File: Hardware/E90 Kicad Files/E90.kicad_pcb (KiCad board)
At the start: 2 copper layers, 93 parts, among them J1 Power Connector Conn_01x02, J10 SDIN Jumper, J11 CS_SDOUT Pre Buffer Test Point, J12 SDOUT Jumper, J13 Audio Connector In Conn_01x03, J14 Conn_02x06_Odd_Even, J15 CS Passthru Jumper Conn_01x02, J16 CS Power Switch Conn_01x02, J17 I2S SDIN Bypass Jumper Conn_0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, J18 PMOD Passthru, J19 I2S SDOUT Bypass Conn_01x02, J2 SWD Connector Conn_02x03, J3 Power Test Point Conn_01x02, J4 BOOT0 Test Point, J6 Audio Connector Out Conn_01x03, J7 MCLK Jumper, J8 WS Jumper, J9 SCLK Jumper, U1 AMS1117-3.3, U2 CS4344_CZZ, U3 NC7SZ125P5, U4 CS5343_CZZ, U5 STM32F407VGT60

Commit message: refactoring PCB
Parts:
- moved C35 214.2 mm to (72.1, 116.1), turned to 180 degrees
- moved C3 206.4 mm to (66.3, 102.3), turned to 270 degrees
- moved C4 204.3 mm to (70.9, 99.6)
- moved FB2 195.6 mm to (66.8, 99.8), turned to 180 degrees
- moved C10 195.2 mm to (77.5, 106.9), turned to 180 degrees
- moved C33 195.0 mm to (77.7, 116.3), turned to 270 degrees
- moved R4 189.8 mm to (90.0, 104.6)
- moved C31 187.4 mm to (87.3, 111.1), turned to 180 degrees
- moved J12 185.3 mm to (75.0, 92.5)
- moved C12 185.1 mm to (92.8, 105.4), turned to 90 degrees
- moved C11 182.5 mm to (92.7, 101.5), turned to 270 degrees
- moved C6 181.3 mm to (84.3, 102.4), turned to 180 degrees
- moved C34 181.1 mm to (75.4, 116.1), turned to 180 degrees
- moved C32 180.9 mm to (87.4, 113.3), turned to 180 degrees
- moved R12 175.0 mm to (89.9, 110.3), turned to 270 degrees
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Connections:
- C23 pad 1: CS_POWER -> +3V3
- C3 pad 1: CS_POWER -> +3V3
- FB2 pad 2: CS_POWER -> +3V3
- FB4 pad 2: CS_POWER -> +3V3
- J6 pad 1: Net-(C12-Pad2) -> Net-(C11-Pad2)
- J6 pad 2: Net-(C11-Pad2) -> Net-(C12-Pad2)
- R11 pad 1: Net-(J13-Pad1) -> Net-(J13-Pad2)
- R9 pad 1: Net-(J13-Pad2) -> Net-(J13-Pad1)
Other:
- board outline added: 50 x 70 mm

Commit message: pcb
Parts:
- removed J16: CS Power Switch Conn_01x02, Connector_PinHeader_2.54mm:PinHeader_1x02_P2.54mm_Vertical
- moved R16 111.3 mm to (58.9, 93.8), turned to 270 degrees
- moved D5 110.5 mm to (60.5, 101.2)
- moved R15 105.6 mm to (60.9, 93.8), turned to 270 degrees
- moved C14 100.7 mm to (64.5, 78.2), turned to 270 degrees
- moved C13 99.9 mm to (63.1, 78.2), turned to 270 degrees
- moved C30 98.3 mm to (64.7, 76.2), turned to 180 degrees
- moved R10 97.8 mm to (68.3, 115.0), turned to 90 degrees
- moved U3 96.3 mm to (63.5, 110.0)
- moved C21 94.2 mm to (64.8, 68.4), turned to 180 degrees
- moved C16 92.5 mm to (69.6, 60.2)
- moved R18 91.6 mm to (54.8, 93.8), turned to 270 degrees
- moved C24 90.3 mm to (79.7, 106.2)
- moved C38 88.7 mm to (60.6, 66.6)
- moved C15 85.9 mm to (65.5, 62.2), turned to 180 degrees
- moved C29 83.9 mm to (64.2, 74.8), turned to 180 degrees
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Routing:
- net +3V3: track 0.00 -> 68.8 mm, vias 0 -> 17
- net CS_MCLK: track 0.00 -> 65.9 mm
- net CS_WS: track 0.00 -> 57.6 mm
- net GND: track 0.00 -> 57.2 mm, vias 0 -> 45
- net CS_CLK: track 0.00 -> 49.6 mm
- net Net-(R18-Pad1): track 0.00 -> 42.1 mm, vias 0 -> 2
- net Net-(R17-Pad2): track 0.00 -> 39.5 mm, vias 0 -> 2
- net Net-(R16-Pad1): track 0.00 -> 37.0 mm, vias 0 -> 2
- net Net-(R15-Pad1): track 0.00 -> 34.3 mm, vias 0 -> 2
- net NRST: track 0.00 -> 34.2 mm, vias 0 -> 1
- net CS_SDOUT: track 0.00 -> 33.0 mm
- net PMOD_CLK: track 0.00 -> 24.9 mm
- net SWO: track 0.00 -> 24.8 mm
- net Net-(D3-Pad2): track 0.00 -> 24.3 mm
- net PMOD_WS: track 0.00 -> 21.5 mm
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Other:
- copper layers 2 -> 4

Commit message: finished pcb 1.0
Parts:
- moved J3 33.8 mm to (54.0, 63.0), turned to 0 degrees
- moved J1 5.42 mm to (57.5, 54.0), turned to 90 degrees
- moved J2 3.99 mm to (93.2, 59.7)
- moved R20 2.65 mm to (75.3, 80.2), turned to 180 degrees
- moved C13 1.45 mm to (64.0, 79.3)
- moved C14 1.26 mm to (65.2, 79.3)
- moved R8 1.19 mm to (66.9, 79.2)
- moved C30 1.17 mm to (64.8, 77.4)
- moved C29 1.07 mm to (64.4, 75.8)
- moved D1 0.76 mm to (59.5, 59.7)
- moved C22 0.72 mm to (64.8, 65.8)
- moved C21 0.60 mm to (65.0, 67.9), turned to 90 degrees
- moved C19 0.49 mm to (69.8, 79.7)
- moved C20 0.46 mm to (64.9, 73.8), turned to 270 degrees
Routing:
- net GND: track 57.2 -> 92.3 mm, vias 45 -> 64
- net PMOD_SDOUT: track 11.6 -> 46.6 mm
- net PMOD_SDIN: track 12.1 -> 35.1 mm
- net +3V3: track 68.8 -> 85.7 mm, vias 17 -> 26
- net CS_SDIN: track 10.4 -> 25.5 mm
- net +3.3VA: track 5.96 -> 14.1 mm
- net SWO: track 24.8 -> 30.0 mm
- net SWDIO: track 17.9 -> 13.6 mm
- net SWCLK: track 15.6 -> 12.1 mm
- net VCC: track 3.64 -> 6.24 mm
- net BOOT1: track 0.00 -> 2.58 mm
- net Net-(C27-Pad1): track 0.00 -> 2.52 mm
- net Net-(C12-Pad2): track 6.00 -> 8.02 mm
- net Net-(C39-Pad1): track 1.99 -> 3.94 mm
- net Net-(C29-Pad1): track 8.74 -> 6.97 mm
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- added copper zone on In2.Cu, net +3V3
- added copper zone on In1.Cu, net GND
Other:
- outline, holes or cut-outs redrawn

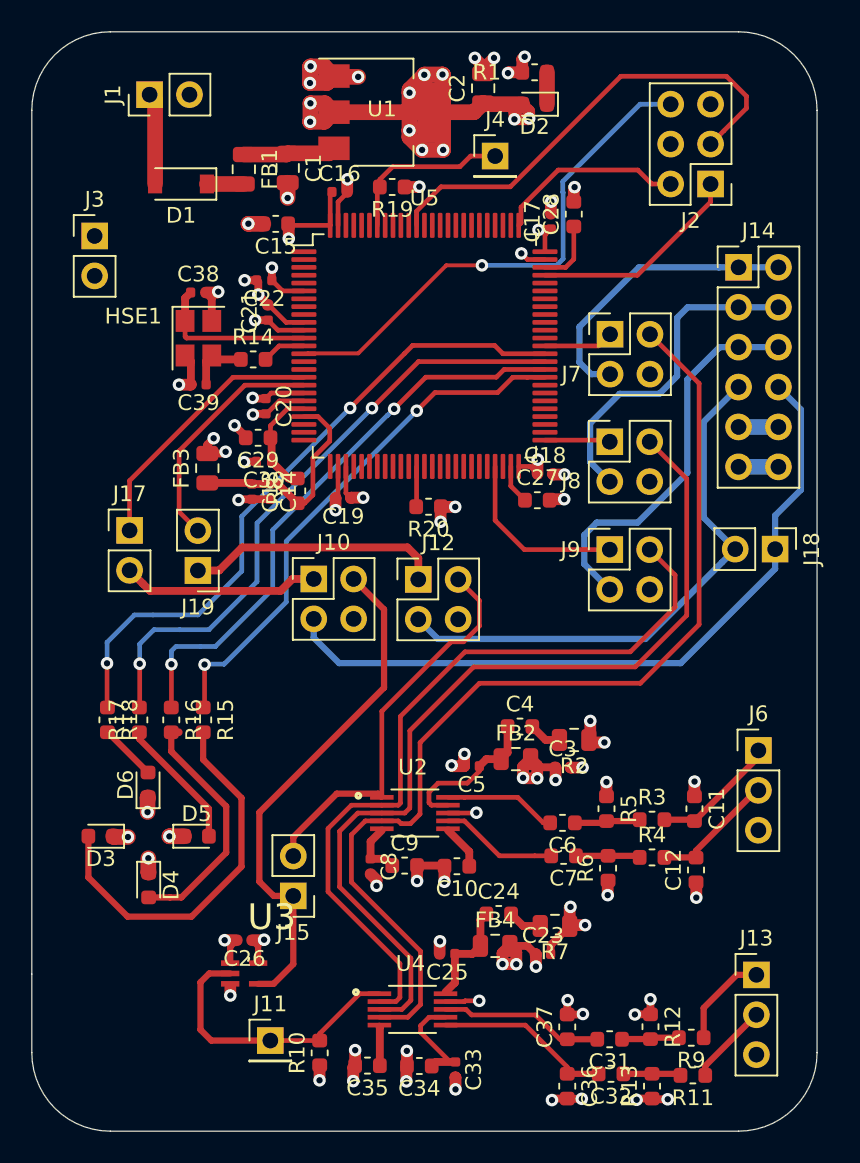
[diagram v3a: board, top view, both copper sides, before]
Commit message: added ground pours on all 4 layers
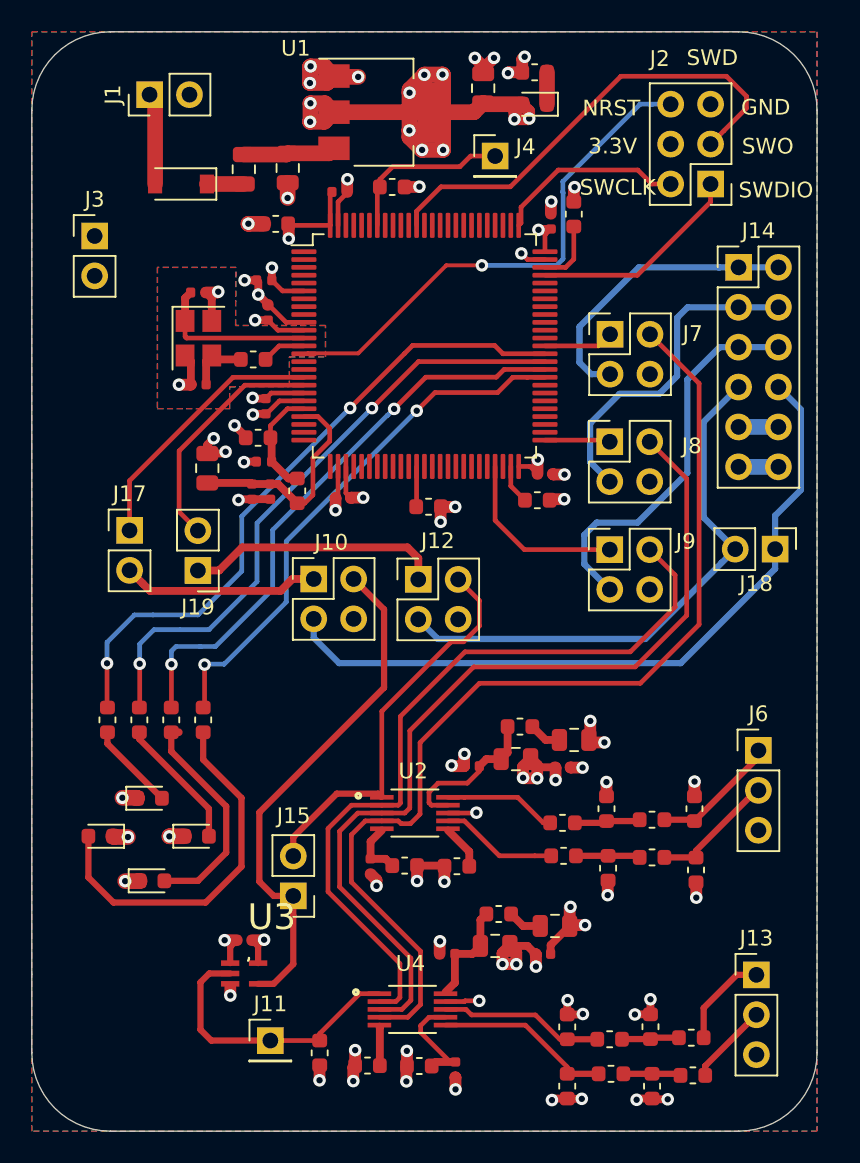
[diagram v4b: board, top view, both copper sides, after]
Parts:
- moved D6 0.86 mm to (57.5, 98.8), turned to 0 degrees
- moved D4 0.34 mm to (57.7, 104.1), turned to 0 degrees
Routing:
- net Net-(D6-Pad2): track 3.65 -> 5.66 mm
- net Net-(D4-Pad2): track 15.7 -> 14.3 mm
- net Net-(D3-Pad2): track 24.3 -> 23.5 mm
- added copper zone on B.Cu, net GND
- added copper zone on F.Cu, net GND
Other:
- board text added: "3.3V"
- board text added: "GND"
- board text added: "NRST"
- board text added: "SWCLK"
- board text added: "SWD"
- board text added: "SWDIO"
- board text added: "SWO"

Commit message: added pdf
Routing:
- removed copper zone on B.Cu, net GND
- removed copper zone on F.Cu, net GND
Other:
- board text added: "+"
- board text added: "3.3V TP"
- board text added: "CS PT"
- board text added: "In"
- board text added: "L"
- board text added: "Out"
- board text added: "PD12"
- board text added: "PD15"
- board text added: "PMOD PT"
- board text added: "R"
- board text added: "VCC"

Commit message: Gerbers finalized for Rev1 znd sent to JLCPCB for fabrication
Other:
- board text added: "E90 1.0 Skyler Cornell"
- board text added: "PD14"
- board text added: "Pre-Buffer TP"
- board text added: "STM32 SDIN"
- board text added: "STM32 SDOUT"
